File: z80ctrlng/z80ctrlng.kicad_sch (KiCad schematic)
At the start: 24 parts, among them J1 RCBus-80, J10 RX_LINK, J2 3V_LINK, J3 TX_LINK, J4 DEBUG, SW1 RESET, SW2 BANK_EN, U1 AS6C4008-55PCN, U2 AVR128DB64x-xPT, U3 74HCT574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

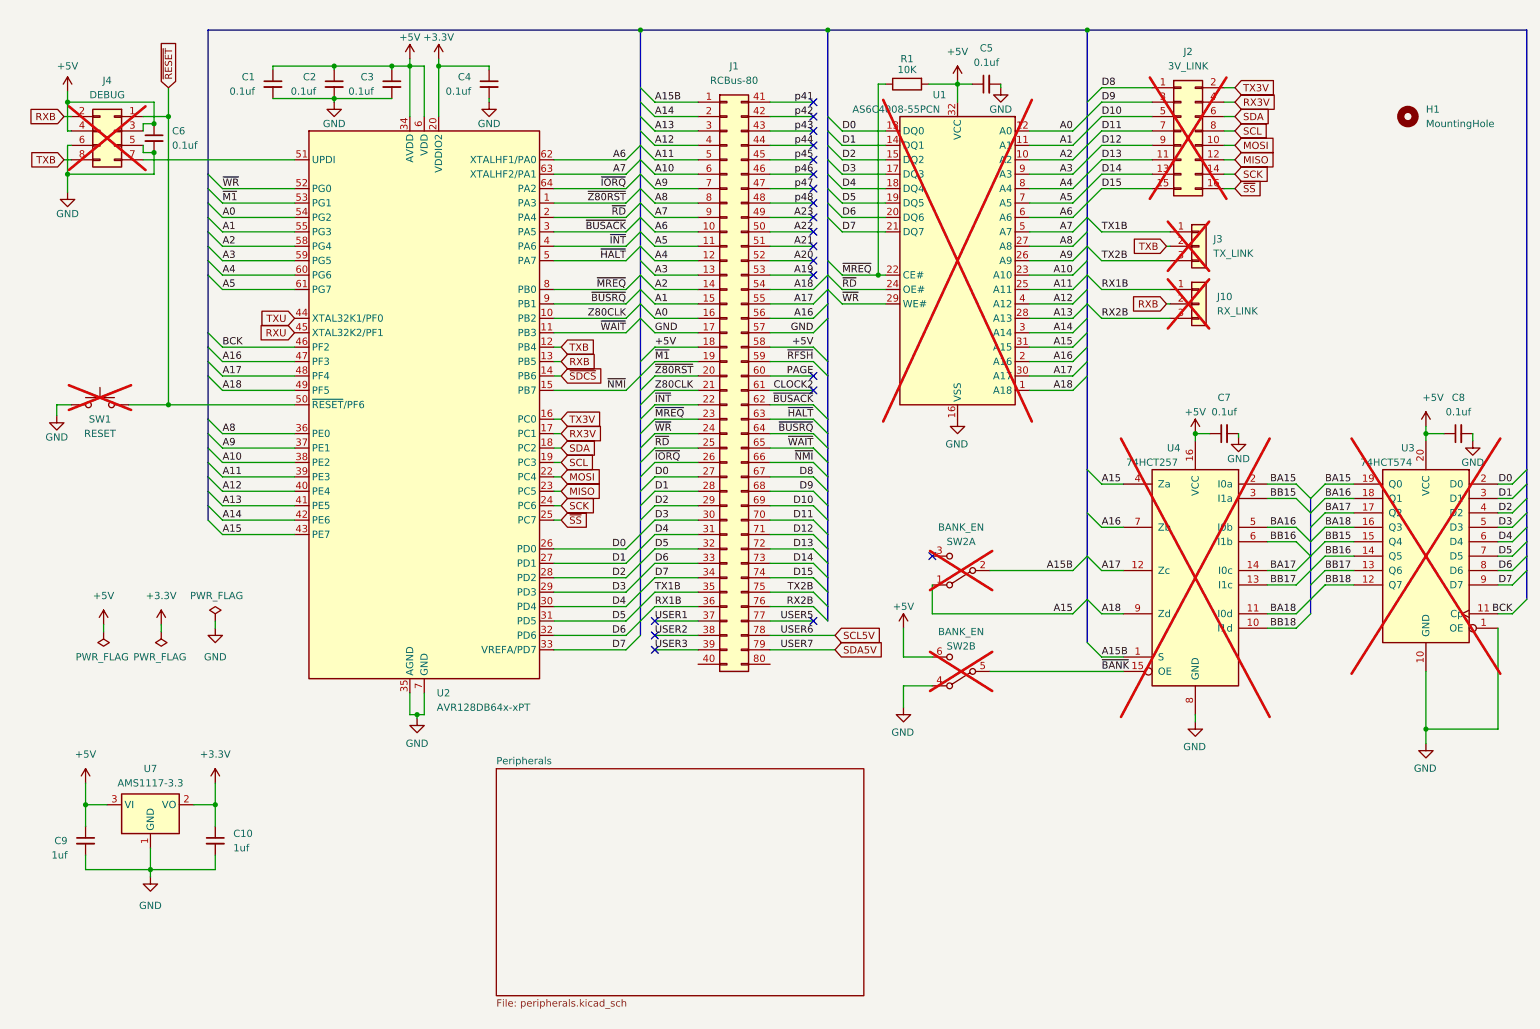
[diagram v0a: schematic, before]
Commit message: Muntz unnecessary jumpers/switches; add SerialUDPI programmer; cleanup layout
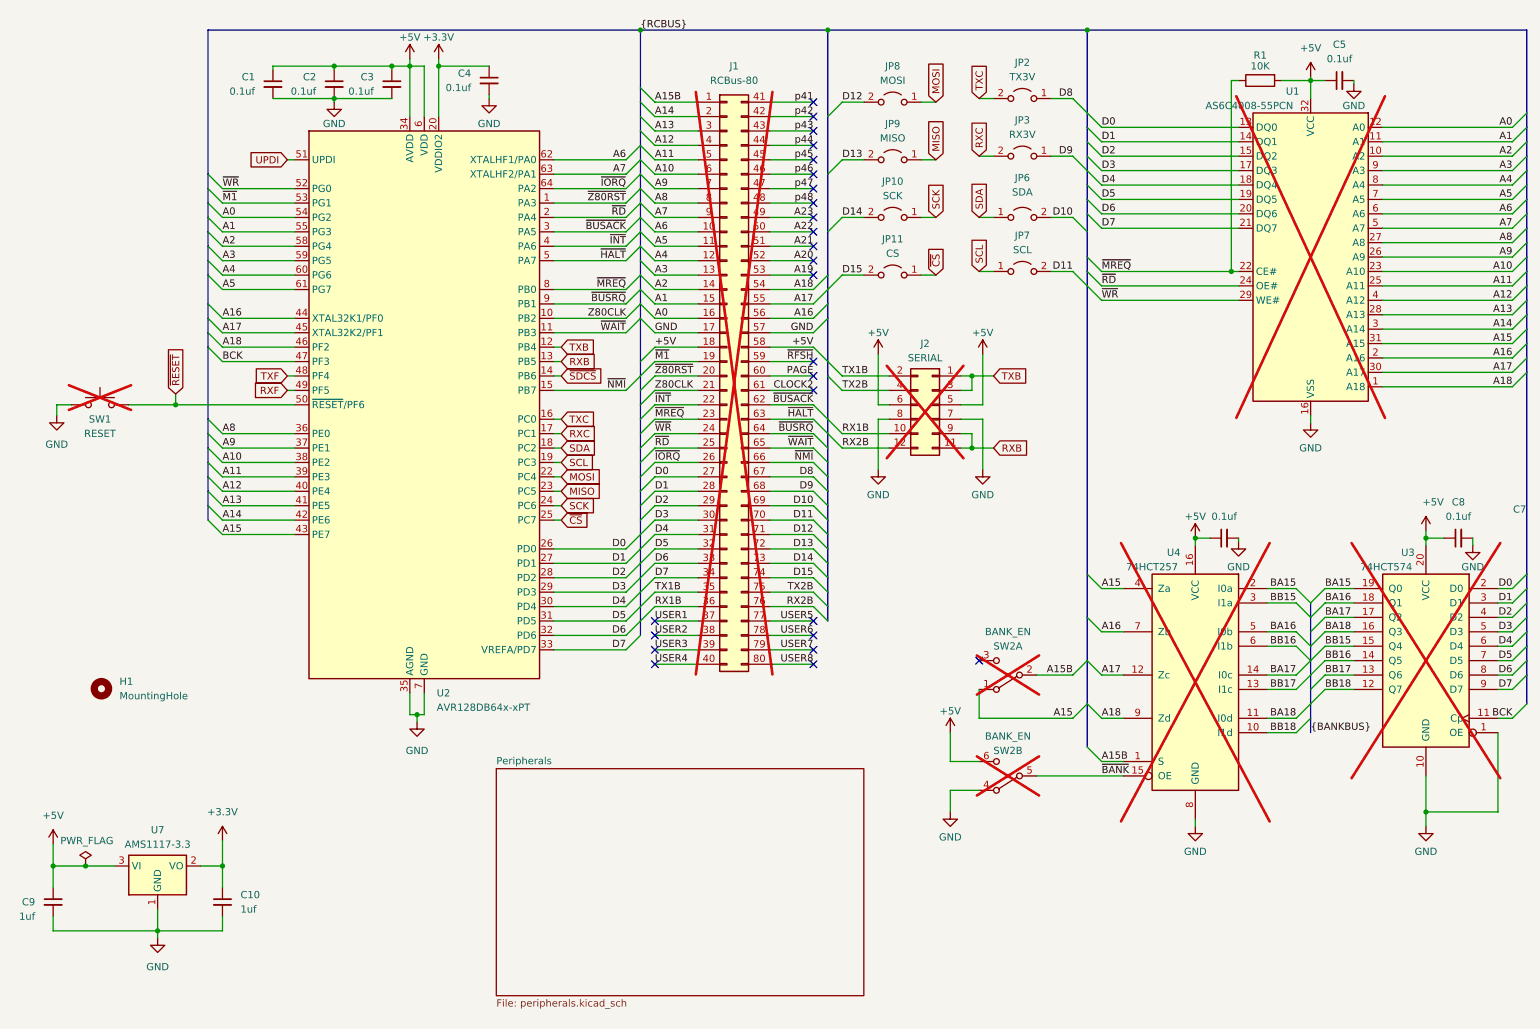
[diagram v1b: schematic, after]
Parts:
- removed C6: 0.1uf, Capacitor_SMD:C_0402_1005Metric, symbol Device:C_Small
- removed J10: RX_LINK, Connector_PinHeader_2.54mm:PinHeader_1x03_P2.54mm_Vertical, symbol Connector_Generic:Conn_01x03
- removed J2: 3V_LINK, Connector_PinHeader_2.54mm:PinHeader_2x08_P2.54mm_Vertical, symbol Connector_Generic:Conn_02x08_Odd_Even
- removed J3: TX_LINK, Connector_PinHeader_2.54mm:PinHeader_1x03_P2.54mm_Vertical, symbol Connector_Generic:Conn_01x03
- removed J4: DEBUG, Connector_PinHeader_2.54mm:PinHeader_2x04_P2.54mm_Horizontal, symbol Connector_Generic:Conn_02x04_Odd_Even
- added J2: SERIAL, Connector_PinHeader_2.54mm:PinHeader_2x06_P2.54mm_Horizontal, symbol Connector_Generic:Conn_02x06_Odd_Even
- added JP10: SCK, Jumper:SolderJumper-2_P1.3mm_Open_RoundedPad1.0x1.5mm, symbol Jumper:Jumper_2_Open
- added JP11: CS, Jumper:SolderJumper-2_P1.3mm_Open_RoundedPad1.0x1.5mm, symbol Jumper:Jumper_2_Open
- added JP2: TX3V, Jumper:SolderJumper-2_P1.3mm_Open_RoundedPad1.0x1.5mm, symbol Jumper:Jumper_2_Open
- added JP3: RX3V, Jumper:SolderJumper-2_P1.3mm_Open_RoundedPad1.0x1.5mm, symbol Jumper:Jumper_2_Open
- added JP6: SDA, Jumper:SolderJumper-2_P1.3mm_Open_RoundedPad1.0x1.5mm, symbol Jumper:Jumper_2_Open
- added JP7: SCL, Jumper:SolderJumper-2_P1.3mm_Open_RoundedPad1.0x1.5mm, symbol Jumper:Jumper_2_Open
- added JP8: MOSI, Jumper:SolderJumper-2_P1.3mm_Open_RoundedPad1.0x1.5mm, symbol Jumper:Jumper_2_Open
- added JP9: MISO, Jumper:SolderJumper-2_P1.3mm_Open_RoundedPad1.0x1.5mm, symbol Jumper:Jumper_2_Open
- J1: now not fitted
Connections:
- net RXU is gone; now on net A17: U2.45 (XTAL32K2/PF1)
- net TXU is gone; now on net A16: U2.44 (XTAL32K1/PF0)
- net +5V: now also J2.5 (Pin_5), J2.6 (Pin_6)
- net A16: no longer U2.47 (PF3)
- net A17: no longer U2.48 (PF4)
- net A18: now also U2.46 (PF2); no longer U2.49 (PF5)
- net BCK: now also U2.47 (PF3); no longer U2.46 (PF2)
- net D10: now also JP6.2 (B)
- net D11: now also JP7.2 (B)
- net D12: now also JP8.2 (B)
- net D13: now also JP9.2 (B)
- net D14: now also JP10.2 (B)
- net D15: now also JP11.2 (B)
- net D8: now also JP2.1 (A)
- net D9: now also JP3.1 (A)
- net GND: now also J2.7 (Pin_7), J2.8 (Pin_8)
- net MISO: now also JP9.1 (A)
- net MOSI: now also JP8.1 (A)
- net RX1B: now also J2.10 (Pin_10)
- net RX2B: now also J2.12 (Pin_12)
- net RXB: now also J2.11 (Pin_11), J2.9 (Pin_9)
- net SCK: now also JP10.1 (A)
- net SCL: now also JP7.1 (A)
- net SDA: now also JP6.1 (A)
- net TX1B: now also J2.2 (Pin_2)
- net TX2B: now also J2.4 (Pin_4)
- net TXB: now also J2.1 (Pin_1), J2.3 (Pin_3)
- net UPDI: now reaches U2.51 (UPDI)
- net USER4: now reaches J1.40 (Pin_40)
- net USER8: now reaches J1.80 (Pin_80)
- net RX3V renamed RXC
- net RXC: now also JP3.2 (B)
- net SCL5V renamed USER6
- net SDA5V renamed USER7
- net TX3V renamed TXC
- net TXC: now also JP2.2 (B)
- net ~{SS} renamed ~{CS}
- net ~{CS}: now also JP11.1 (A)
- new net RXF: U2.49 (PF5)
- new net TXF: U2.48 (PF4)
- no-connect marks 20 -> 25
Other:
- moved on the sheet: C10, C4, C5, C7, C8, C9, H1, R1, SW2A, SW2B, U1, U3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

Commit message: Rearrange to make fast 3.3V buses shorter
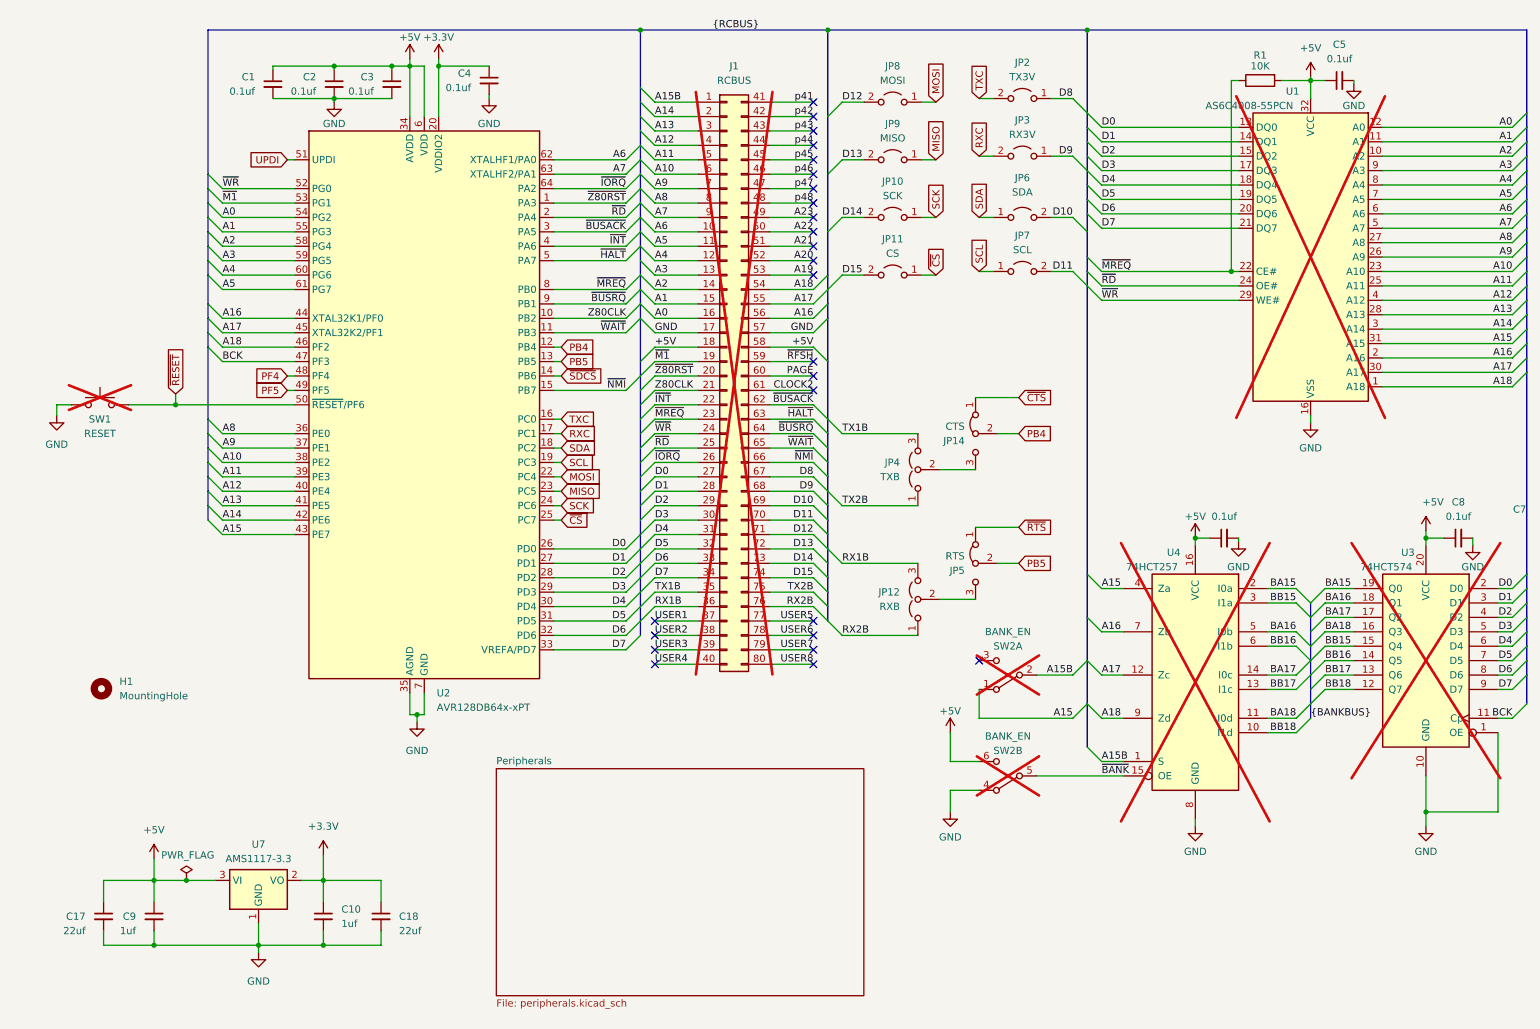
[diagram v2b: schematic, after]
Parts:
- removed J2: SERIAL, Connector_PinHeader_2.54mm:PinHeader_2x06_P2.54mm_Horizontal, symbol Connector_Generic:Conn_02x06_Odd_Even
- added C17, C18: 22uf, Capacitor_SMD:C_1206_3216Metric, symbol Device:C_Small
- added JP12: RXB, Jumper:SolderJumper-3_P1.3mm_Open_RoundedPad1.0x1.5mm, symbol Jumper:Jumper_3_Open
- added JP14: CTS, Jumper:SolderJumper-3_P1.3mm_Bridged12_RoundedPad1.0x1.5mm, symbol Jumper:Jumper_3_Bridged12
- added JP4: TXB, Jumper:SolderJumper-3_P1.3mm_Open_RoundedPad1.0x1.5mm, symbol Jumper:Jumper_3_Open
- added JP5: RTS, Jumper:SolderJumper-3_P1.3mm_Bridged12_RoundedPad1.0x1.5mm, symbol Jumper:Jumper_3_Bridged12
- J1: value RCBus-80 -> RCBUS
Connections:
- net +3.3V: now also C18.1
- net +5V: now also C17.1
- net GND: now also C17.2, C18.2
- net RX1B: now also JP12.3 (B)
- net RX2B: now also JP12.1 (A)
- net TX1B: now also JP4.3 (B)
- net TX2B: now also JP4.1 (A)
- net RXB renamed PB5
- net PB5: now also JP5.2 (C)
- net RXF renamed PF5
- net TXB renamed PB4
- net PB4: now also JP14.2 (C)
- net TXF renamed PF4
- new net: JP12.2 (C), JP5.3 (B)
- new net: JP14.3 (B), JP4.2 (C)
- new net ~{CTS}: JP14.1 (A)
- new net ~{RTS}: JP5.1 (A)
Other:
- moved on the sheet: C10, C9, U7

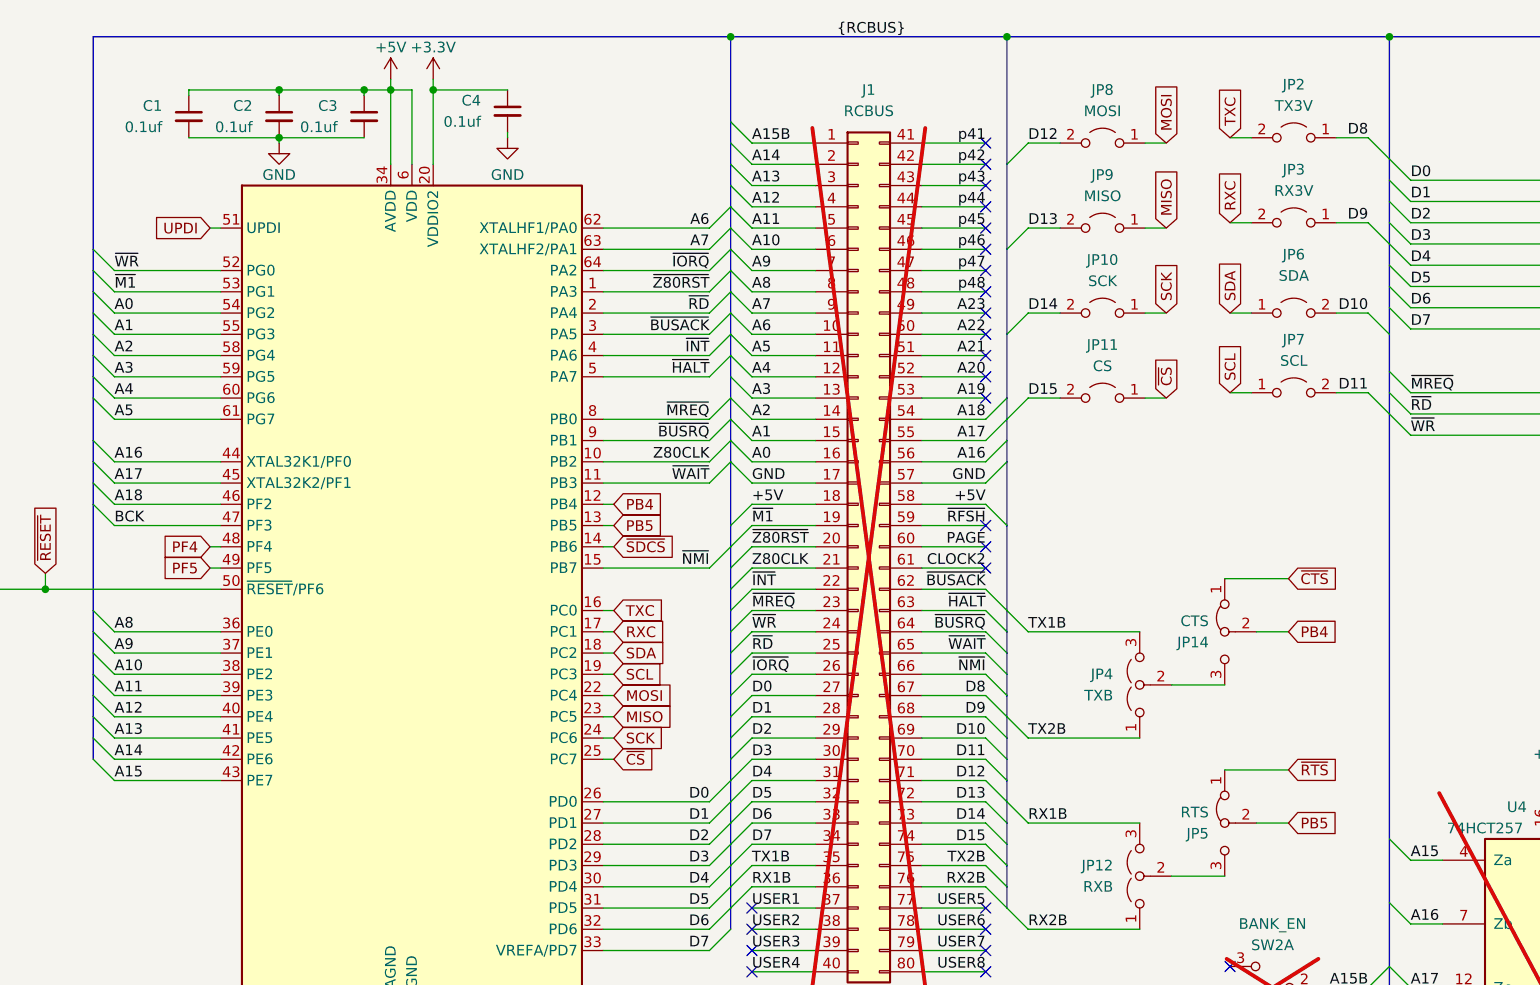
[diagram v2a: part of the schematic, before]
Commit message: Updating silkscreen
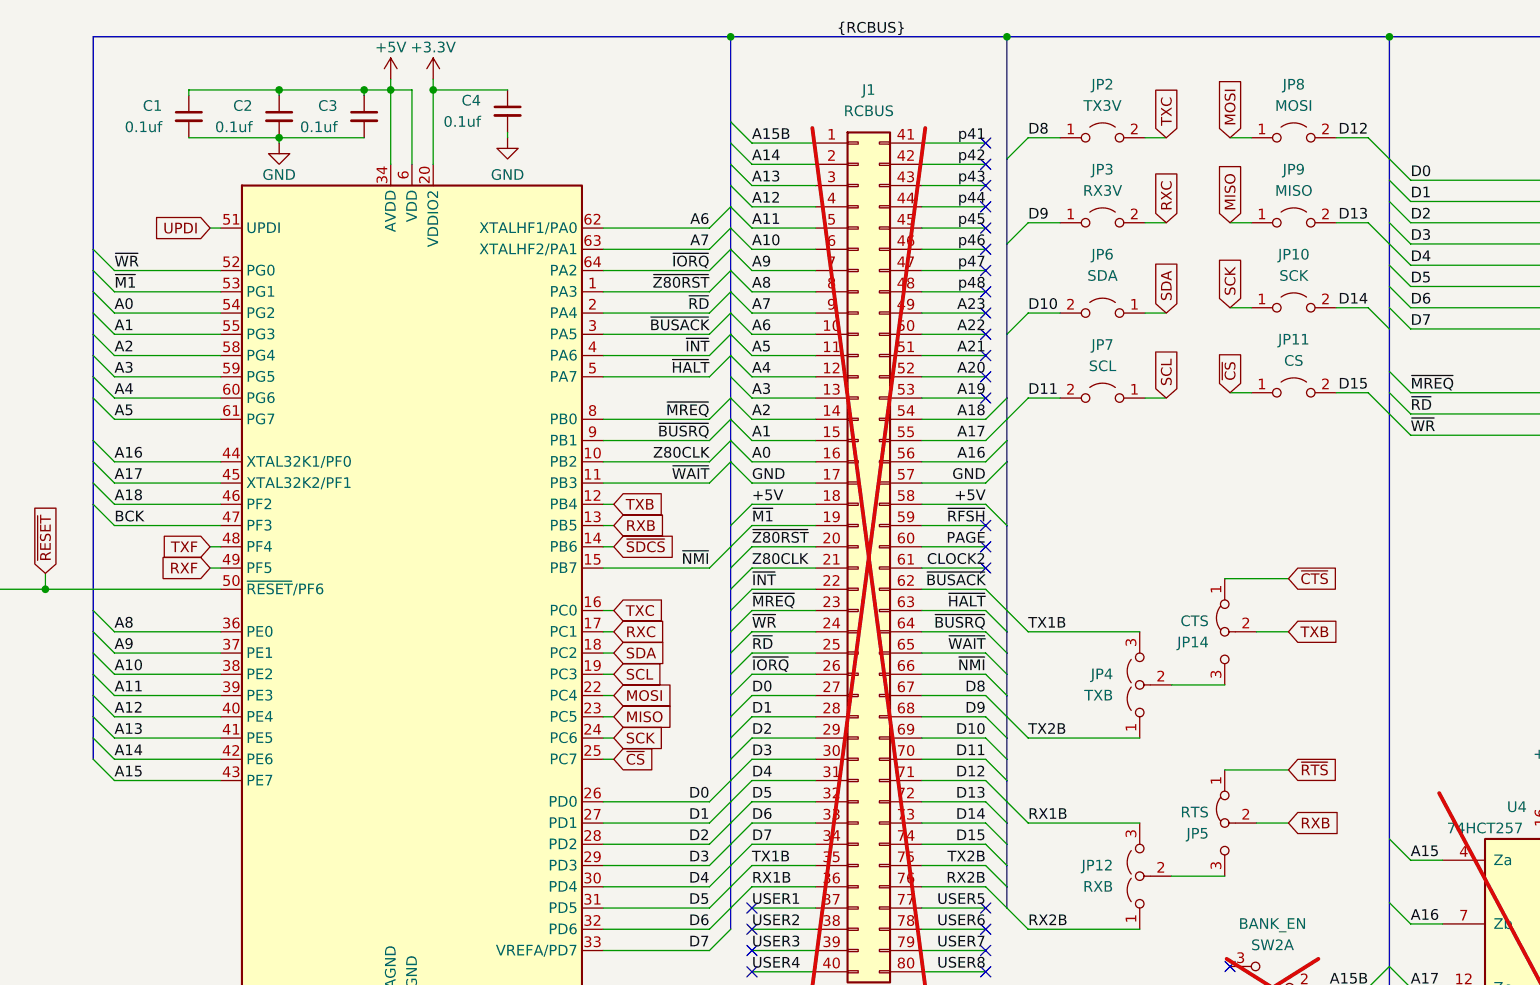
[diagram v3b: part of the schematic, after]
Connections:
- net PB4 renamed TXB
- net PB5 renamed RXB
- net PF4 renamed TXF
- net PF5 renamed RXF
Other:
- moved on the sheet: JP10, JP11, JP2, JP3, JP6, JP7, JP8, JP9
